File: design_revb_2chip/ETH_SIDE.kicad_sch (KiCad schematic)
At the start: 54 parts, among them J3 09452812810, U4 DP83TG720SWRHARQ1, U5 TPS784105QWDRBRQ1

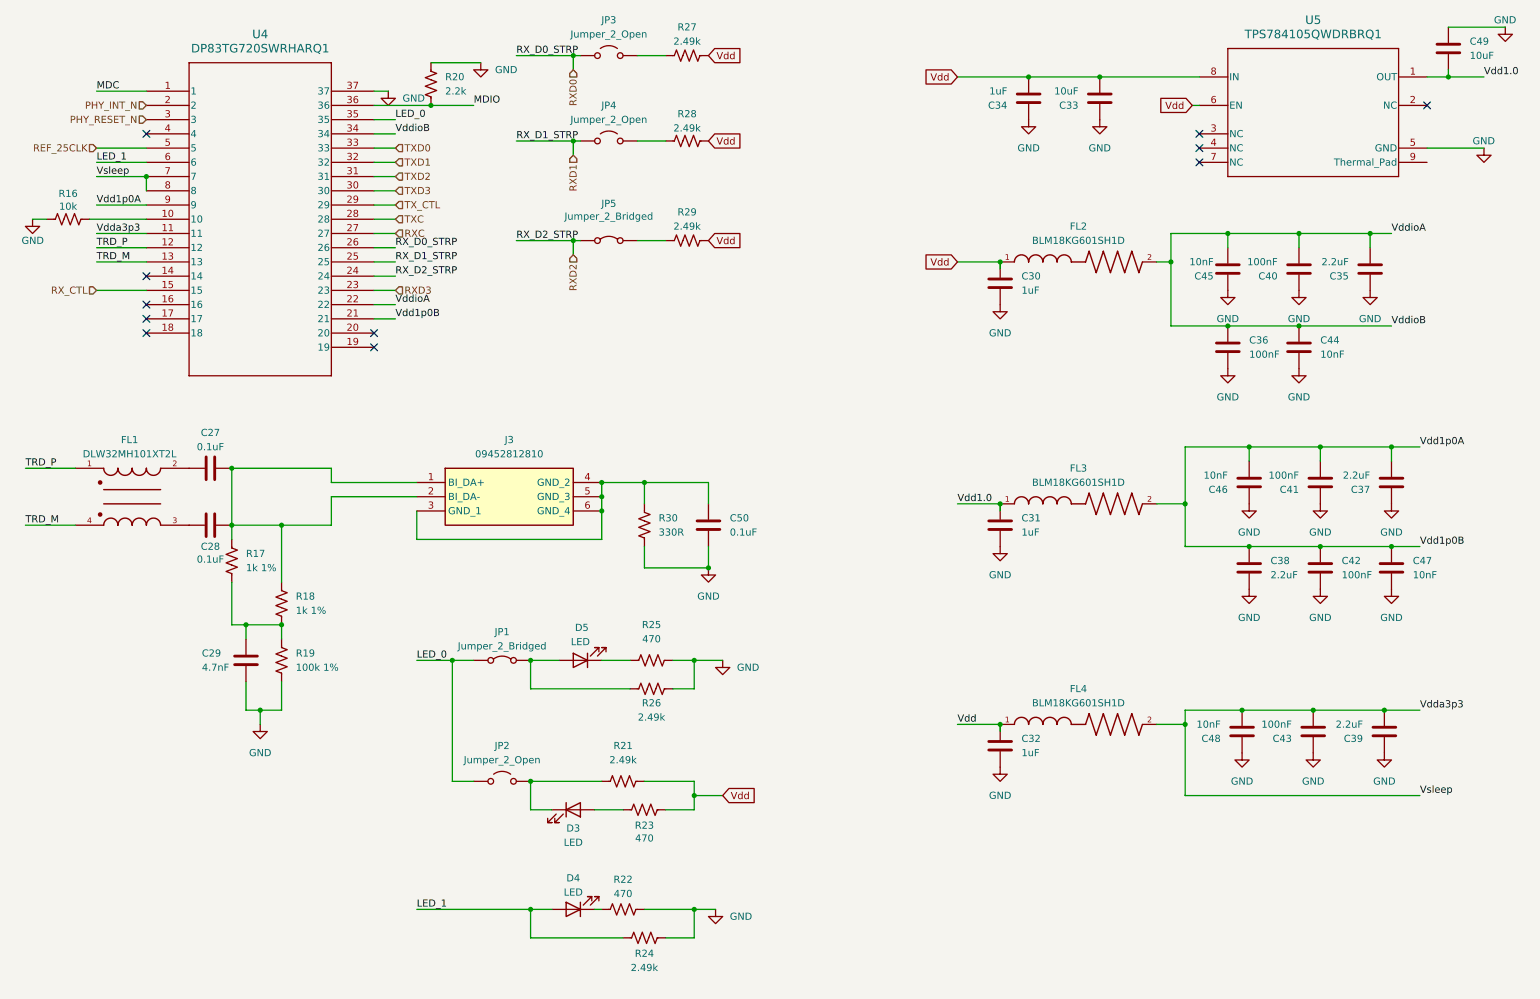
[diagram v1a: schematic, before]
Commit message: added dip switch block
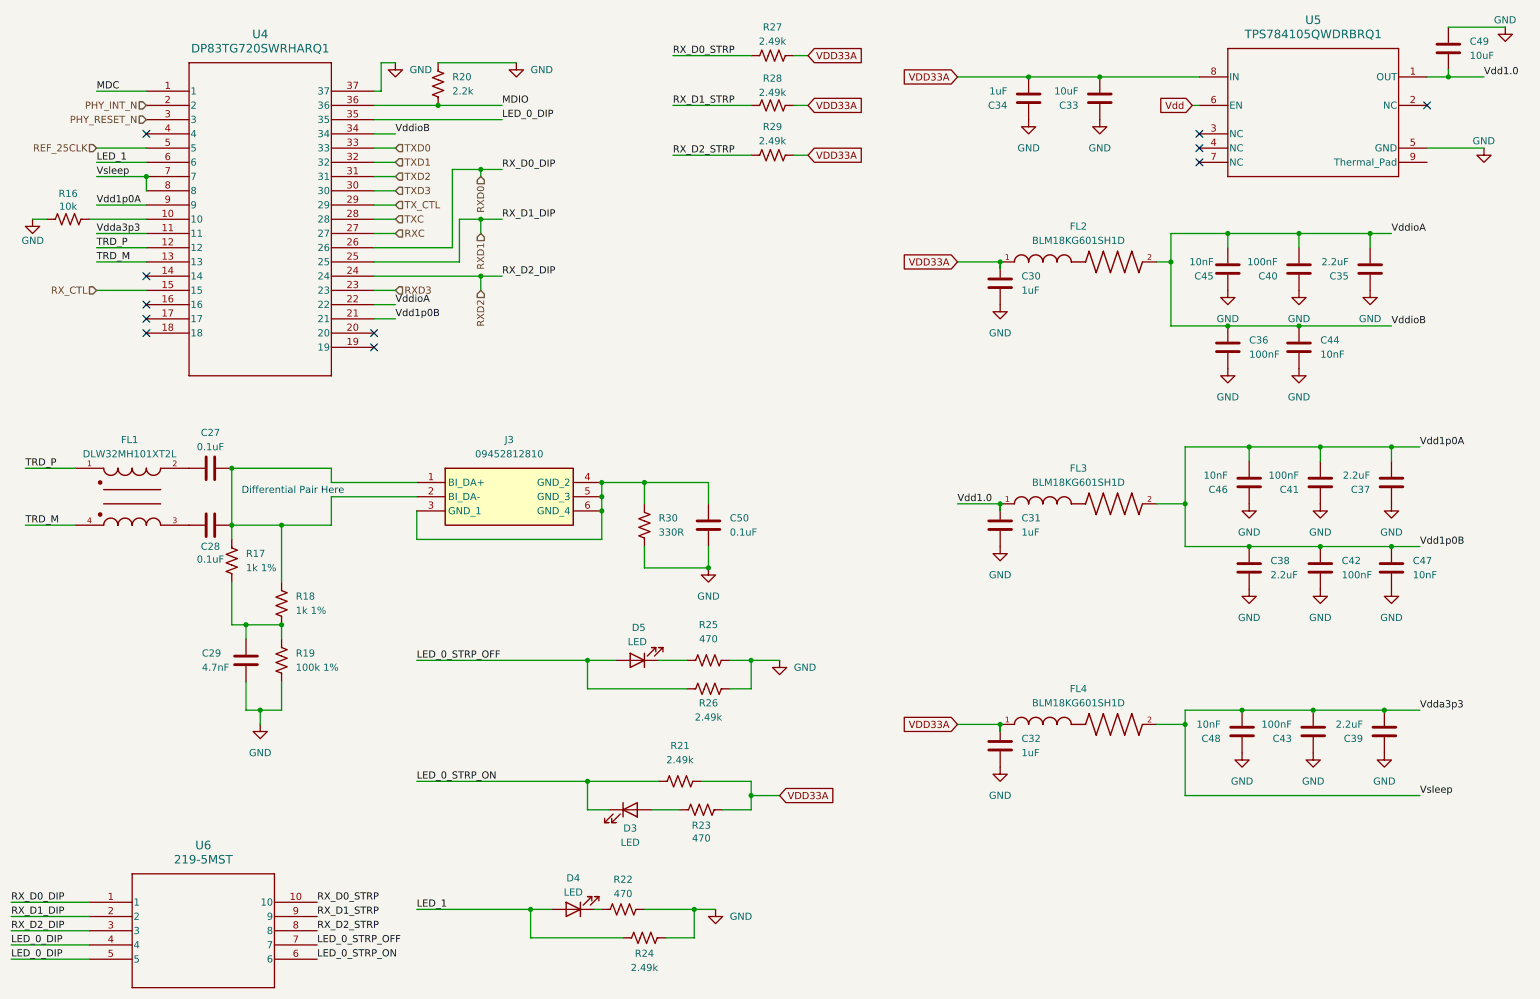
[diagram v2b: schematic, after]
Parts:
- removed JP1, JP5: Jumper_2_Bridged, Jumper:SolderJumper-2_P1.3mm_Bridged_Pad1.0x1.5mm, symbol Jumper:Jumper_2_Bridged
- removed JP2, JP3, JP4: Jumper_2_Open, Jumper:SolderJumper-3_P1.3mm_Open_Pad1.0x1.5mm, symbol Jumper:Jumper_2_Open
- added U6: 219-5MST, SW5_219SMT, symbol Capstone_Synbols:219-5MST
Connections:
- net RXD0: now also U6.1
- net RXD1: now also U6.2
- net RXD2: now also U6.3
- net Vdd: no longer C30.1, C32.1, C33.2, C34.2, FL2.1, FL4.1, R21.2, R23.2, R27.1, R28.1, R29.1, U5.8 (IN)
- net LED_0_STRP_OFF: now reaches D5.2 (A), R26.1
- net LED_0_STRP_OFF: now also U6.7
- net RX_D2_STRP: now reaches R29.2
- net RX_D2_STRP: now also U6.8
- net RX_D0_STRP: now reaches R27.2
- net RX_D0_STRP: now also U6.10
- net LED_0_STRP_ON: now reaches D3.1 (K), R21.1
- net LED_0_STRP_ON: now also U6.6
- net RX_D1_STRP: now reaches R28.2
- net RX_D1_STRP: now also U6.9
- net LED_0 renamed LED_0_DIP
- net LED_0_DIP: now also U6.4, U6.5
- new net VDD33A: C30.1, C32.1, C33.2, C34.2, FL2.1, FL4.1, R21.2, R23.2, R27.1, R28.1, R29.1, U5.8 (IN)
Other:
- note added: "Differential Pair Here"
- moved on the sheet: D3, D5, R20, R21, R23, R25, R26, R27, R28, R29

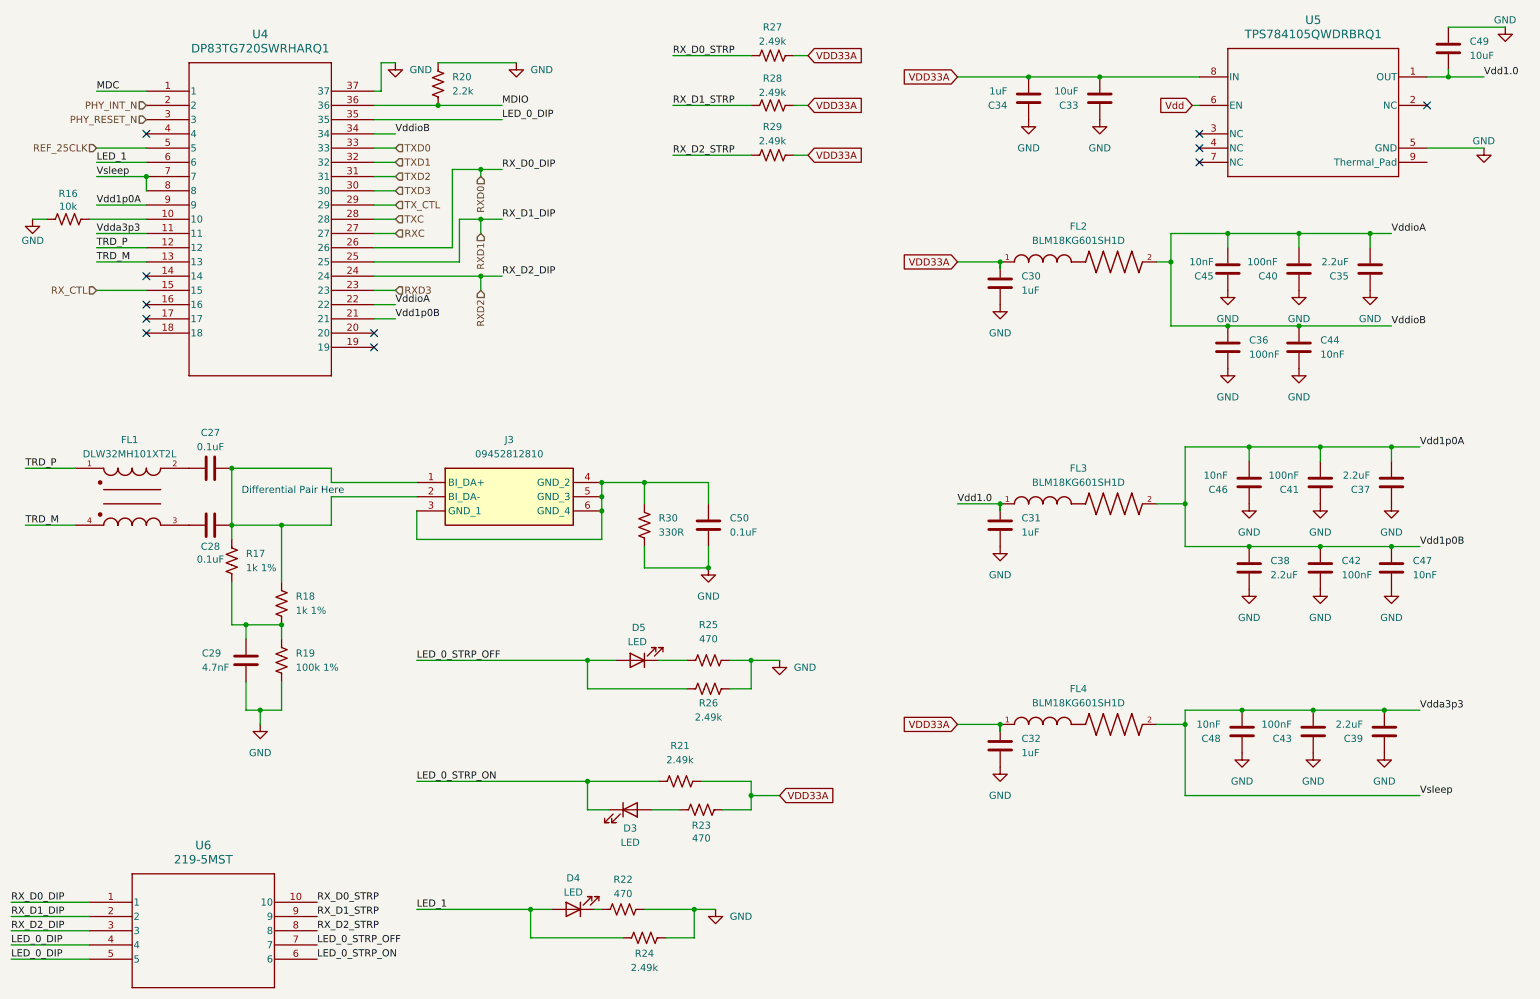
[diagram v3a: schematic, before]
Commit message: routing eth side
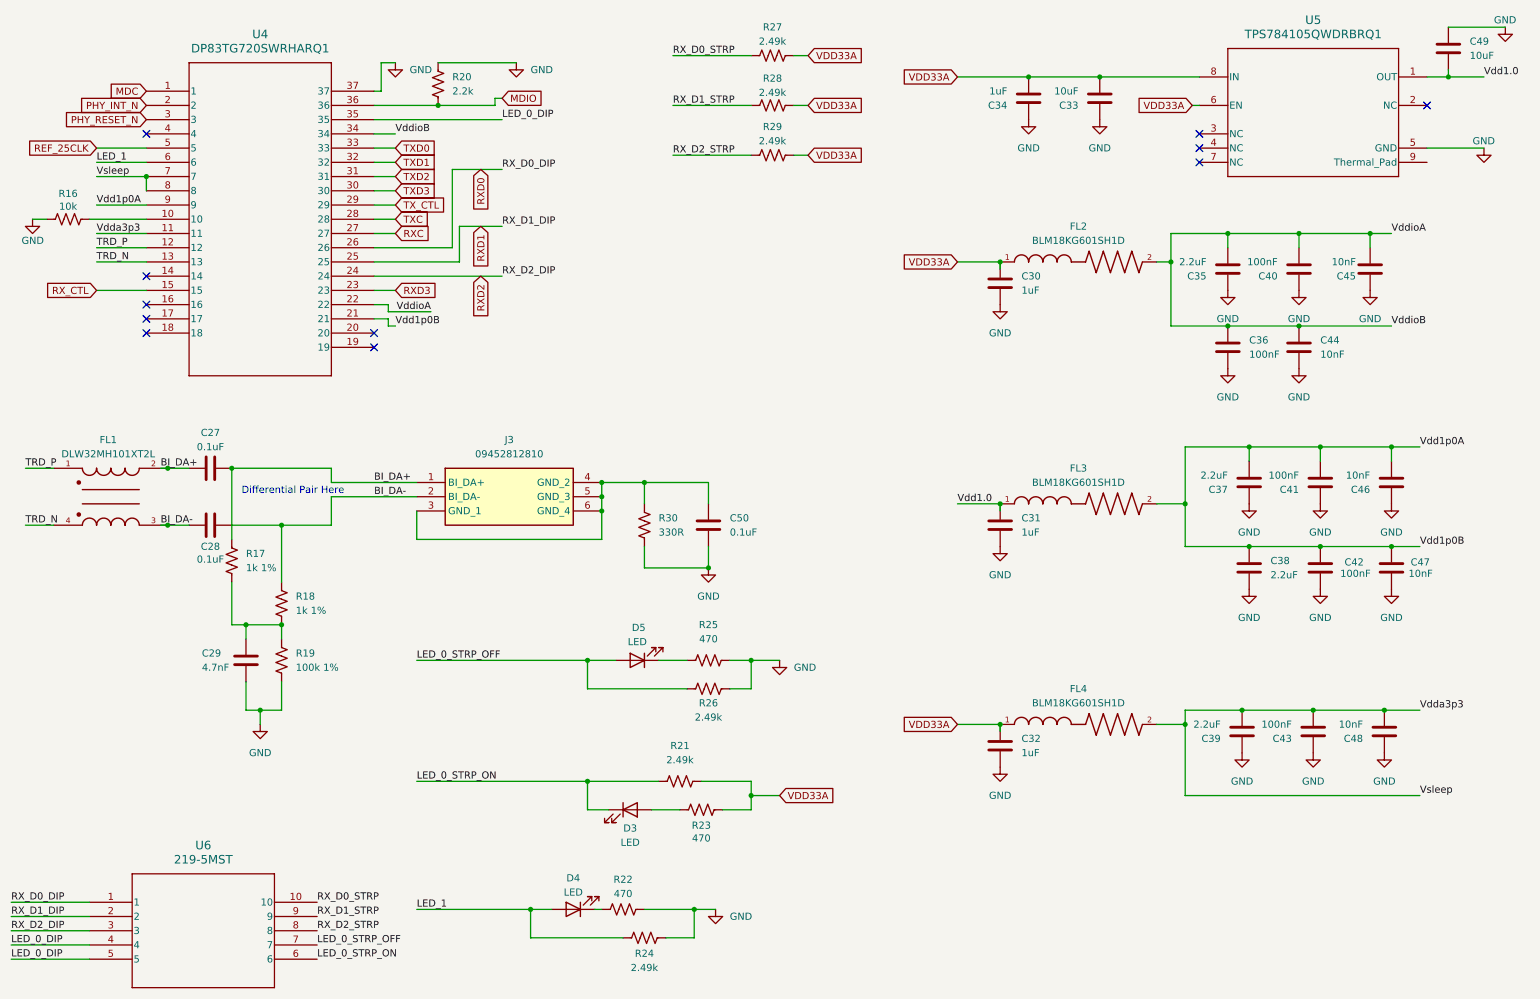
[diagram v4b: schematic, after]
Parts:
- C50: footprint (none) -> Capacitor_SMD:C_0201_0603Metric
- FL1: footprint DLW32MH101XT2L:FIL_DLW32MH101XT2L -> Capstone_Footprints:FIL_DLW32MH101XT2L
- FL2, FL3, FL4: footprint BLM18KG601SH1D:BEADC1608X95N -> Capstone_Footprints:BEADC1608X95N
- R30: footprint Capacitor_SMD:C_0201_0603Metric -> Resistor_SMD:R_0805_2012Metric
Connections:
- net Vdd is gone; now on net VDD33A: U5.6 (EN)
- net BI_DA+: now reaches C27.1, FL1.2
- net BI_DA+: now also C27.2, J3.1 (BI_DA+), R17.1
- net BI_DA-: now reaches C28.1, J3.2 (BI_DA-), R18.1
- net BI_DA-: now also C28.2, FL1.3; no longer C27.2, J3.1 (BI_DA+), R17.1
- net TRD_M renamed TRD_N
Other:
- moved on the sheet: FL1

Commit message: Final PCB Fixes
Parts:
- U6: footprint SW5_219SMT -> Capstone_Footprints:SW5_219SMT
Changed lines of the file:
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@@
 			)
 		)
-		(property "Footprint" "SW5_219SMT"
+		(property "Footprint" "Capstone_Footprints:SW5_219SMT"
 			(at 26.67 175.26 0)
 			(effects

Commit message: PCB Fixes/Completion
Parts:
- J3: footprint Capstone_Footprints:09452812810 -> Capstone_Footprints:hartingt1
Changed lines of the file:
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@@
 			)
 		)
-		(property "Footprint" "Capstone_Footprints:09452812810"
+		(property "Footprint" "Capstone_Footprints:hartingt1"
 			(at 114.3 195.25 0)
 			(effects
